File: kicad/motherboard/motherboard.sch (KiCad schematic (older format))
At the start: 21 parts, among them J1 DB37_Female, J10 DB37_Female, J11 DB37_Female, J12 Barrel_Jack, J13 TSR 1-2433, J2 DB37_Female, J3 DB37_Female, J4 DB37_Female, J5 DB37_Female, J6 DB25_Female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

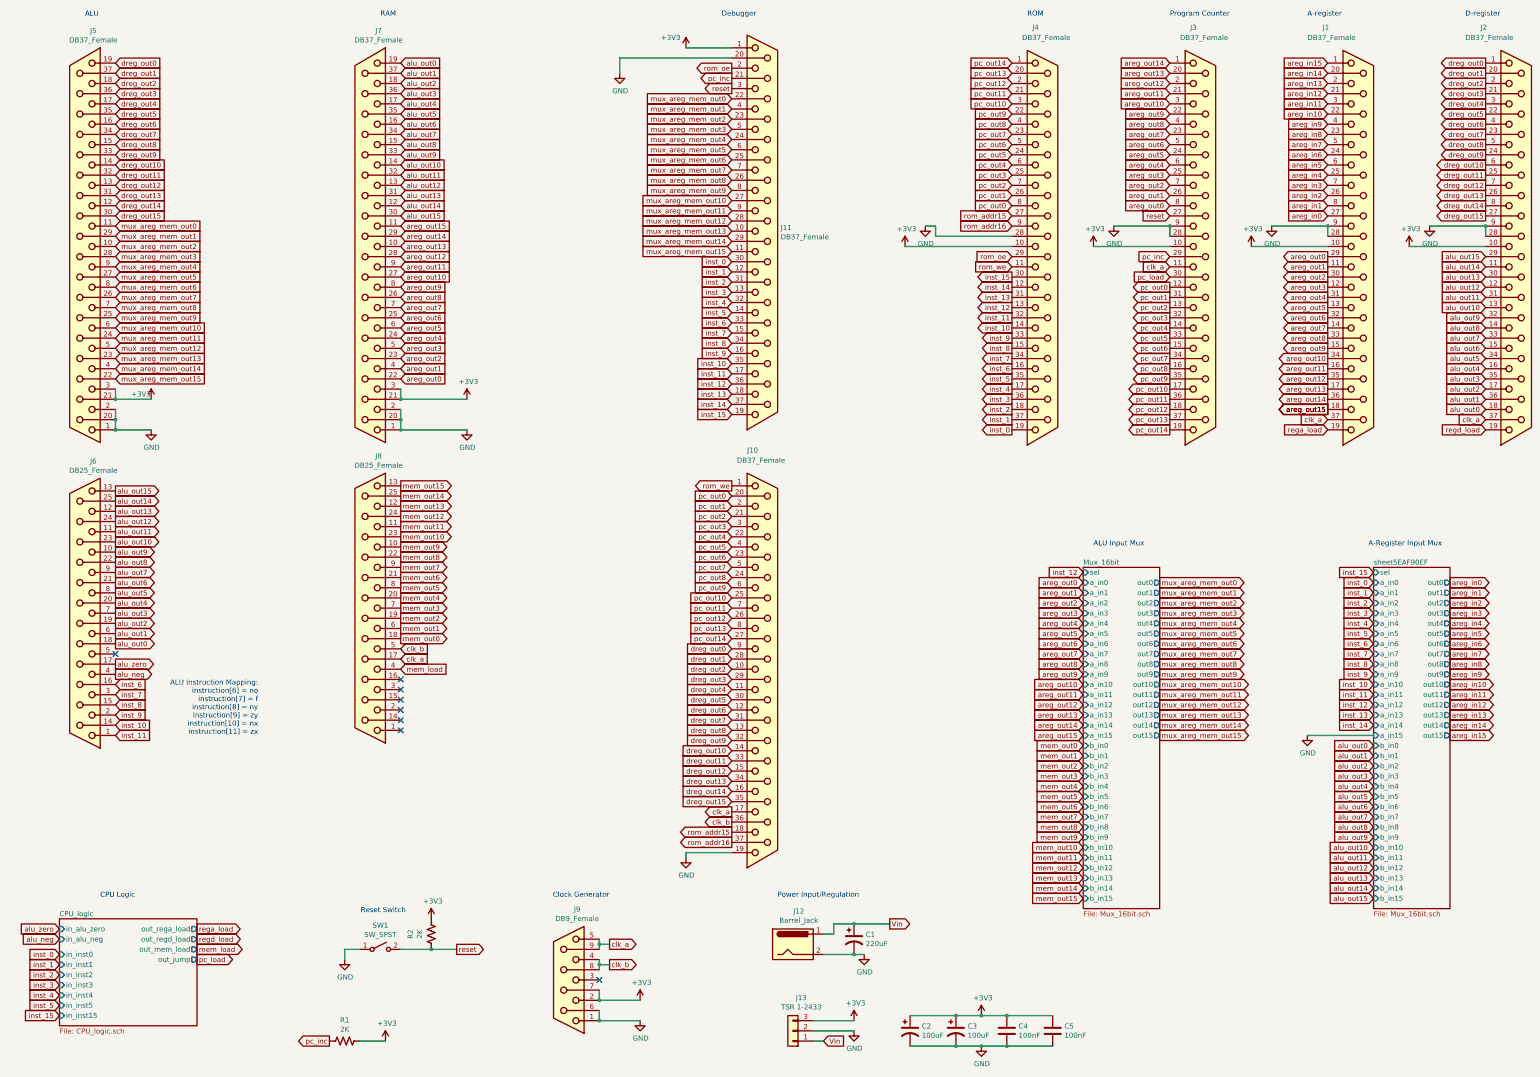
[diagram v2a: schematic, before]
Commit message: Ram (#5)
* Flipped clk A and B based on timing diagram. Added output buffers for clock signals.

* Added clock output enable signal to motherboard debugger. Updated component library.

* Schematic and layout for RAM board complete.

* ALU schematic complete, ready for layout and routing.

* ALU layout, routing complete. Associated motherboard mod. 

* Added Load LED to register and program counter boards.
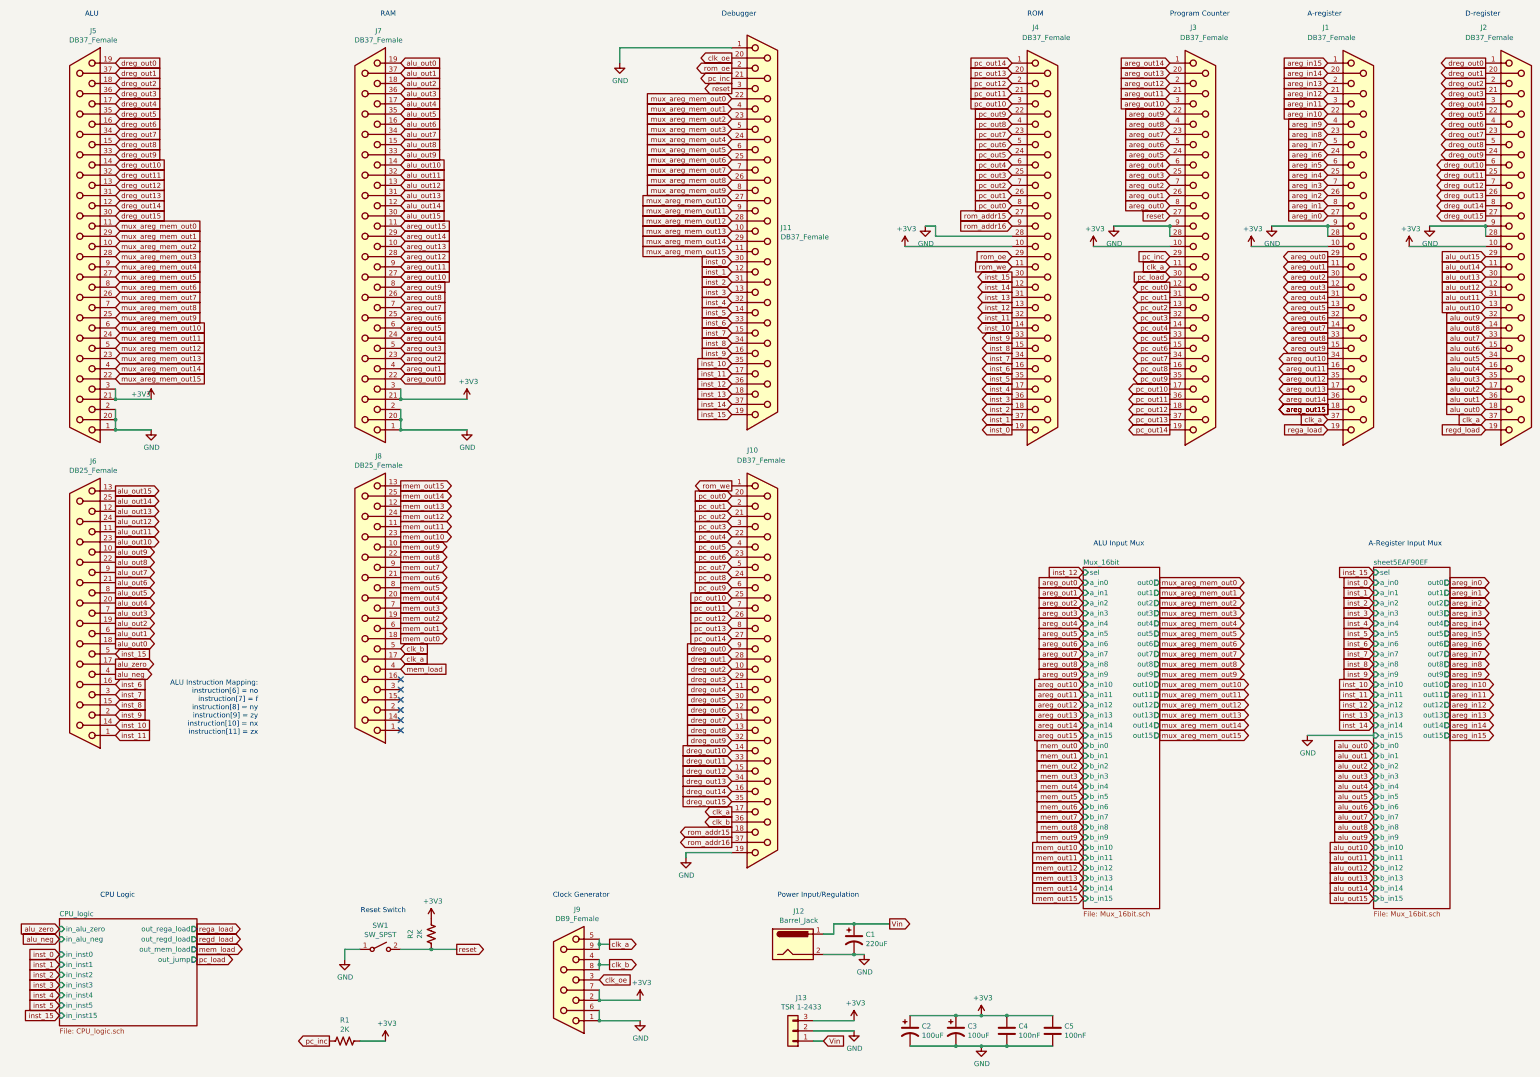
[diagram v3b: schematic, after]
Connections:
- net +3V3: no longer J11.1
- net GND: now also J11.1; no longer J11.20
- net inst_15: now also J6.5
- net clk_oe: now reaches J9.3
- net clk_oe: now also J11.20
- no-connect marks 8 -> 6
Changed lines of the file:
@@
 	6500 10500 6900 10500
 Connection ~ 6500 10500
-NoConn ~ 6500 10100
 $Sheet
 S 11250 6050 750  3350
@@
 L power:GND #PWR052
 U 1 1 5E99FE8F
-P 6700 1200
-F 0 "#PWR052" H 6700 950 50  0001 C CNN
-F 1 "GND" H 6705 1027 50  0000 C CNN
-F 2 "" H 6700 1200 50  0001 C CNN
-F 3 "" H 6700 1200 50  0001 C CNN
-	1    6700 1200
-	1    0    0    -1
-$EndComp
-Wire Wire Line
-	7800 950  7350 950
-$Comp
-L power:+3V3 #PWR051
-U 1 1 5E9A1A48
-P 7350 950
-F 0 "#PWR051" H 7350 800 50  0001 C CNN
-F 1 "+3V3" H 7200 1050 50  0000 C CNN
-F 2 "" H 7350 950 50  0001 C CNN
-F 3 "" H 7350 950 50  0001 C CNN
-	1    7350 950
+P 6700 1100
+F 0 "#PWR052" H 6700 850 50  0001 C CNN
+F 1 "GND" H 6705 927 50  0000 C CNN
+F 2 "" H 6700 1100 50  0001 C CNN
+F 3 "" H 6700 1100 50  0001 C CNN
+	1    6700 1100
 	1    0    0    -1
 $EndComp
@@
 	1    0    0    -1
 $EndComp
-NoConn ~ 1750 6900
 $Comp
 L Device:CP1 C2
@@
 	7800 8850 7350 8850
 Wire Wire Line
-	7800 1050 6700 1050
-Wire Wire Line
-	6700 1050 6700 1200
+	7800 950  6700 950
+Wire Wire Line
+	6700 950  6700 1100
+Text GLabel 6500 10100 2    50   Input ~ 0
+clk_oe
+Text GLabel 7800 1050 0    50   Output ~ 0
+clk_oe
+Text GLabel 1750 6900 2    50   Input ~ 0
+inst_15
 $EndSCHEMATC

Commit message: Readme updates (#6)
* Readme intro section

* Board revisions for manufacturing, add digikey PNs to all, added logo.
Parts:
- J1, J10, J11, J2, J3, J4, J5, J7: footprint Connector_Dsub:DSUB-37_Female_Horizontal_P2.77x2.84mm_EdgePinOffset4.94mm_Housed_MountingHolesOffset7.48mm -> Connector_Dsub:DSUB-37_Female_Horizontal_P2.77x2.84mm_EdgePinOffset7.70mm_Housed_MountingHolesOffset9.12mm; Digikey PN (none) -> AE10941-ND
- J12: Digikey PN (none) -> CP-063AH-ND
- J13: Digikey PN (none) -> 1951-2430-ND
- J6, J8: footprint Connector_Dsub:DSUB-25_Female_Horizontal_P2.77x2.84mm_EdgePinOffset4.94mm_Housed_MountingHolesOffset7.48mm -> Connector_Dsub:DSUB-25_Female_Horizontal_P2.77x2.84mm_EdgePinOffset7.70mm_Housed_MountingHolesOffset9.12mm; Digikey PN (none) -> AE10935-ND
- J9: footprint Connector_Dsub:DSUB-9_Female_Horizontal_P2.77x2.84mm_EdgePinOffset4.94mm_Housed_MountingHolesOffset7.48mm -> Connector_Dsub:DSUB-9_Female_Horizontal_P2.77x2.84mm_EdgePinOffset7.70mm_Housed_MountingHolesOffset9.12mm; Digikey PN (none) -> AE10921-ND
- R1, R2: Digikey PN (none) -> P2.0KECT-ND
- SW1: Digikey PN (none) -> SW415-ND
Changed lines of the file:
@@
 F 0 "J2" H 15150 5050 50  0000 L CNN
 F 1 "DB37_Female" H 15000 4950 50  0000 L CNN
-F 2 "Connector_Dsub:DSUB-37_Female_Horizontal_P2.77x2.84mm_EdgePinOffset4.94mm_Housed_MountingHolesOffset7.48mm" H 15500 2900 50  0001 C CNN
+F 2 "Connector_Dsub:DSUB-37_Female_Horizontal_P2.77x2.84mm_EdgePinOffset7.70mm_Housed_MountingHolesOffset9.12mm" H 15500 2900 50  0001 C CNN
 F 3 " ~" H 15500 2900 50  0001 C CNN
+F 4 "AE10941-ND" H 15500 2900 50  0001 C CNN "Digikey PN"
 	1    15500 2900
 	1    0    0    -1
@@
 F 0 "J1" H 13600 5050 50  0000 L CNN
 F 1 "DB37_Female" H 13450 4950 50  0000 L CNN
-F 2 "Connector_Dsub:DSUB-37_Female_Horizontal_P2.77x2.84mm_EdgePinOffset4.94mm_Housed_MountingHolesOffset7.48mm" H 13950 2900 50  0001 C CNN
+F 2 "Connector_Dsub:DSUB-37_Female_Horizontal_P2.77x2.84mm_EdgePinOffset7.70mm_Housed_MountingHolesOffset9.12mm" H 13950 2900 50  0001 C CNN
 F 3 " ~" H 13950 2900 50  0001 C CNN
+F 4 "AE10941-ND" H 13950 2900 50  0001 C CNN "Digikey PN"
 	1    13950 2900
 	1    0    0    -1
@@
 F 0 "J3" H 12300 5050 50  0000 L CNN
 F 1 "DB37_Female" H 12200 4950 50  0000 L CNN
-F 2 "Connector_Dsub:DSUB-37_Female_Horizontal_P2.77x2.84mm_EdgePinOffset4.94mm_Housed_MountingHolesOffset7.48mm" H 12400 2900 50  0001 C CNN
+F 2 "Connector_Dsub:DSUB-37_Female_Horizontal_P2.77x2.84mm_EdgePinOffset7.70mm_Housed_MountingHolesOffset9.12mm" H 12400 2900 50  0001 C CNN
 F 3 " ~" H 12400 2900 50  0001 C CNN
+F 4 "AE10941-ND" H 12400 2900 50  0001 C CNN "Digikey PN"
 	1    12400 2900
 	1    0    0    -1
@@
 F 0 "J4" H 10750 5050 50  0000 L CNN
 F 1 "DB37_Female" H 10650 4950 50  0000 L CNN
-F 2 "Connector_Dsub:DSUB-37_Female_Horizontal_P2.77x2.84mm_EdgePinOffset4.94mm_Housed_MountingHolesOffset7.48mm" H 10850 2900 50  0001 C CNN
+F 2 "Connector_Dsub:DSUB-37_Female_Horizontal_P2.77x2.84mm_EdgePinOffset7.70mm_Housed_MountingHolesOffset9.12mm" H 10850 2900 50  0001 C CNN
 F 3 " ~" H 10850 2900 50  0001 C CNN
+F 4 "AE10941-ND" H 10850 2900 50  0001 C CNN "Digikey PN"
 	1    10850 2900
 	1    0    0    -1
@@
 F 0 "J5" H 1368 783 50  0000 C CNN
 F 1 "DB37_Female" H 1368 874 50  0000 C CNN
-F 2 "Connector_Dsub:DSUB-37_Female_Horizontal_P2.77x2.84mm_EdgePinOffset4.94mm_Housed_MountingHolesOffset7.48mm" H 1450 2900 50  0001 C CNN
+F 2 "Connector_Dsub:DSUB-37_Female_Horizontal_P2.77x2.84mm_EdgePinOffset7.70mm_Housed_MountingHolesOffset9.12mm" H 1450 2900 50  0001 C CNN
 F 3 " ~" H 1450 2900 50  0001 C CNN
+F 4 "AE10941-ND" H 1450 2900 50  0001 C CNN "Digikey PN"
 	1    1450 2900
 	-1   0    0    1
@@
 F 0 "J6" H 1368 5008 50  0000 C CNN
 F 1 "DB25_Female" H 1368 5099 50  0000 C CNN
-F 2 "Connector_Dsub:DSUB-25_Female_Horizontal_P2.77x2.84mm_EdgePinOffset4.94mm_Housed_MountingHolesOffset7.48mm" H 1450 6500 50  0001 C CNN
+F 2 "Connector_Dsub:DSUB-25_Female_Horizontal_P2.77x2.84mm_EdgePinOffset7.70mm_Housed_MountingHolesOffset9.12mm" H 1450 6500 50  0001 C CNN
 F 3 " ~" H 1450 6500 50  0001 C CNN
+F 4 "AE10935-ND" H 1450 6500 50  0001 C CNN "Digikey PN"
 	1    1450 6500
 	-1   0    0    1
@@
 F 0 "J9" H 6118 9408 50  0000 C CNN
 F 1 "DB9_Female" H 6118 9499 50  0000 C CNN
-F 2 "Connector_Dsub:DSUB-9_Female_Horizontal_P2.77x2.84mm_EdgePinOffset4.94mm_Housed_MountingHolesOffset7.48mm" H 6200 10100 50  0001 C CNN
+F 2 "Connector_Dsub:DSUB-9_Female_Horizontal_P2.77x2.84mm_EdgePinOffset7.70mm_Housed_MountingHolesOffset9.12mm" H 6200 10100 50  0001 C CNN
 F 3 " ~" H 6200 10100 50  0001 C CNN
+F 4 "AE10921-ND" H 6200 10100 50  0001 C CNN "Digikey PN"
 	1    6200 10100
 	-1   0    0    1
@@
 F 2 "Resistor_SMD:R_1206_3216Metric" V 4040 10690 50  0001 C CNN
 F 3 "~" H 4000 10700 50  0001 C CNN
+F 4 "P2.0KECT-ND" V 4000 10700 50  0001 C CNN "Digikey PN"
 	1    4000 10700
 	0    1    1    0
@@
 F 0 "J10" H 7950 9200 50  0000 L CNN
 F 1 "DB37_Female" H 7850 9100 50  0000 L CNN
-F 2 "Connector_Dsub:DSUB-37_Female_Horizontal_P2.77x2.84mm_EdgePinOffset4.94mm_Housed_MountingHolesOffset7.48mm" H 8100 7050 50  0001 C CNN
+F 2 "Connector_Dsub:DSUB-37_Female_Horizontal_P2.77x2.84mm_EdgePinOffset7.70mm_Housed_MountingHolesOffset9.12mm" H 8100 7050 50  0001 C CNN
 F 3 " ~" H 8100 7050 50  0001 C CNN
+F 4 "AE10941-ND" H 8100 7050 50  0001 C CNN "Digikey PN"
 	1    8100 7050
 	1    0    0    -1
@@
 F 0 "J11" H 8280 2784 50  0000 L CNN
 F 1 "DB37_Female" H 8280 2693 50  0000 L CNN
-F 2 "Connector_Dsub:DSUB-37_Female_Horizontal_P2.77x2.84mm_EdgePinOffset4.94mm_Housed_MountingHolesOffset7.48mm" H 8100 2750 50  0001 C CNN
+F 2 "Connector_Dsub:DSUB-37_Female_Horizontal_P2.77x2.84mm_EdgePinOffset7.70mm_Housed_MountingHolesOffset9.12mm" H 8100 2750 50  0001 C CNN
 F 3 " ~" H 8100 2750 50  0001 C CNN
+F 4 "AE10941-ND" H 8100 2750 50  0001 C CNN "Digikey PN"
 	1    8100 2750
 	1    0    0    -1
@@
 F 2 "Button_Switch_SMD:SW_SPST_B3S-1000" H 4350 9800 50  0001 C CNN
 F 3 "~" H 4350 9800 50  0001 C CNN
+F 4 "SW415-ND" H 4350 9800 50  0001 C CNN "Digikey PN"
 	1    4350 9800
 	1    0    0    -1
@@
 F 2 "Resistor_SMD:R_1206_3216Metric" V 4890 9640 50  0001 C CNN
 F 3 "~" H 4850 9650 50  0001 C CNN
+F 4 "P2.0KECT-ND" V 4850 9650 50  0001 C CNN "Digikey PN"
 	1    4850 9650
 	1    0    0    -1
@@
 F 2 "Connector_BarrelJack:BarrelJack_CUI_PJ-063AH_Horizontal" H 8450 9710 50  0001 C CNN
 F 3 "~" H 8450 9710 50  0001 C CNN
+F 4 "CP-063AH-ND" H 8400 9750 50  0001 C CNN "Digikey PN"
 	1    8400 9750
 	1    0    0    -1
@@
 F 2 "Connector_PinHeader_2.54mm:PinHeader_1x03_P2.54mm_Vertical" H 8400 10600 50  0001 C CNN
 F 3 "~" H 8400 10600 50  0001 C CNN
+F 4 "1951-2430-ND" H 8400 10600 50  0001 C CNN "Digikey PN"
 	1    8400 10600
 	-1   0    0    1
@@
 F 0 "J7" H 4168 783 50  0000 C CNN
 F 1 "DB37_Female" H 4168 874 50  0000 C CNN
-F 2 "Connector_Dsub:DSUB-37_Female_Horizontal_P2.77x2.84mm_EdgePinOffset4.94mm_Housed_MountingHolesOffset7.48mm" H 4250 2900 50  0001 C CNN
+F 2 "Connector_Dsub:DSUB-37_Female_Horizontal_P2.77x2.84mm_EdgePinOffset7.70mm_Housed_MountingHolesOffset9.12mm" H 4250 2900 50  0001 C CNN
 F 3 " ~" H 4250 2900 50  0001 C CNN
+F 4 "AE10941-ND" H 4250 2900 50  0001 C CNN "Digikey PN"
 	1    4250 2900
 	-1   0    0    1
@@
 F 0 "J8" H 4168 4958 50  0000 C CNN
 F 1 "DB25_Female" H 4168 5049 50  0000 C CNN
-F 2 "Connector_Dsub:DSUB-25_Female_Horizontal_P2.77x2.84mm_EdgePinOffset4.94mm_Housed_MountingHolesOffset7.48mm" H 4250 6450 50  0001 C CNN
+F 2 "Connector_Dsub:DSUB-25_Female_Horizontal_P2.77x2.84mm_EdgePinOffset7.70mm_Housed_MountingHolesOffset9.12mm" H 4250 6450 50  0001 C CNN
 F 3 " ~" H 4250 6450 50  0001 C CNN
+F 4 "AE10935-ND" H 4250 6450 50  0001 C CNN "Digikey PN"
 	1    4250 6450
 	-1   0    0    1
